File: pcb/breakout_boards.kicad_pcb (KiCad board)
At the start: 2 copper layers, 26.8 x 20 mm, 91 parts, among them J1 Conn_01x04, J2 Conn_01x04, J3 Conn_01x04, J4 Conn_01x04, J5 Conn_01x04, J6 Conn_01x04, J7 Conn_01x04, J8 Conn_01x04, J9 Conn_01x04, SW1 SW_Push_45deg, SW10 SW_Push_45deg, SW11 SW_Push_45deg, SW12 SW_Push_45deg, SW13 SW_Push_45deg, SW14 SW_Push_45deg, SW15 SW_Push_45deg, SW16 SW_Push_45deg, SW17 SW_Push_45deg, SW18 SW_Push_45deg, SW19 SW_Push_45deg, SW2 SW_Push_45deg, SW20 SW_Push_45deg, SW21 SW_Push_45deg, SW22 SW_Push_45deg, SW23 SW_Push_45deg, SW24 SW_Push_45deg, SW25 SW_Push_45deg, SW26 SW_Push_45deg, SW27 SW_Push_45deg, SW28 SW_Push_45deg, SW29 SW_Push_45deg, SW3 SW_Push_45deg, SW30 SW_Push_45deg, SW31 SW_Push_45deg, SW32 SW_Push_45deg, SW4 SW_Push_45deg, SW5 SW_Push_45deg, SW6 SW_Push_45deg, SW7 SW_Push_45deg, SW8 SW_Push_45deg, SW9 SW_Push_45deg

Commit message: almost done
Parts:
- removed J2: Conn_01x04, Connector_PinHeader_2.54mm:PinHeader_1x04_P2.54mm_Vertical
- added H2: MountingHole, Panelization:mouse-bite-3mm-slot, F.Cu at (45.5, 22.0)
- added H3: MountingHole, Panelization:mouse-bite-3mm-slot, F.Cu at (21.8, 33.2)
- added H4: MountingHole, Panelization:mouse-bite-3mm-slot, F.Cu at (22.0, 41.0)
- added H5: MountingHole, Panelization:mouse-bite-3mm-slot, F.Cu at (50.8, 41.0)
- added H6: MountingHole, Panelization:mouse-bite-3mm-slot, F.Cu at (38.0, 31.2)
- added H7: MountingHole, Panelization:mouse-bite-3mm-slot, F.Cu at (38.0, 41.0)
- added H8: MountingHole, Panelization:mouse-bite-3mm-slot, F.Cu at (45.5, 35.8)
- J1: value Conn_01x04 -> Conn_01x05; footprint Connector_PinHeader_2.54mm:PinHeader_1x04_P2.54mm_Vertical -> Connector_PinHeader_2.54mm:PinHeader_1x05_P2.54mm_Vertical
- J6, J7: moved to B.Cu
- moved SW8 132.3 mm to (47.0, 57.4)
- moved SW7 126.6 mm to (37.0, 57.4)
- moved J6 124.6 mm to (31.4, 44.5), turned to -90 degrees
- moved SW6 122.0 mm to (27.0, 57.4)
- moved SW16 119.7 mm to (47.0, 73.3)
- moved SW5 118.8 mm to (17.0, 57.4)
- moved SW15 115.5 mm to (37.0, 73.3)
- moved SW14 112.6 mm to (27.0, 73.3)
- moved SW13 111.3 mm to (17.0, 73.3)
- moved SW4 106.8 mm to (47.0, 49.4)
- moved SW3 101.9 mm to (37.0, 49.4)
- moved J7 100.8 mm to (31.4, 82.6), turned to -90 degrees
- moved SW2 98.5 mm to (27.0, 49.4)
- moved SW1 96.8 mm to (17.0, 49.4)
- moved SW12 95.2 mm to (47.0, 65.3)
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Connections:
- D2 pad 1: Net-(D2-K) -> Net-(D1-K)
- D3 pad 1: Net-(D3-K) -> Net-(D1-K)
- D4 pad 1: Net-(D4-K) -> Net-(D1-K)
- J1 pad 1: Net-(J1-Pin_1) -> Net-(D1-K)
- J4 pad 1: Net-(J4-Pin_1) -> /led_matrix.r3
- J4 pad 2: Net-(J4-Pin_2) -> /led_matrix.r2
- J4 pad 3: Net-(J4-Pin_3) -> /led_matrix.r1
- J4 pad 4: Net-(J4-Pin_4) -> /led_matrix.r0
- J5 pad 1: /led_matrix.c3 -> Net-(J5-Pin_1)
- J5 pad 2: /led_matrix.c2 -> Net-(J5-Pin_2)
- J5 pad 3: /led_matrix.c1 -> Net-(J5-Pin_3)
- J5 pad 4: /led_matrix.c0 -> Net-(J5-Pin_4)
- R1 pad 1: Net-(J1-Pin_4) -> Net-(J1-Pin_2)
- R3 pad 1: Net-(J1-Pin_2) -> Net-(J1-Pin_4)
- R4 pad 1: Net-(J1-Pin_1) -> Net-(J1-Pin_5)
- R5 pad 1: Net-(J4-Pin_3) -> /led_matrix.c1
- R5 pad 2: /led_matrix.r1 -> Net-(J5-Pin_3)
- R7 pad 1: Net-(J4-Pin_2) -> /led_matrix.c2
- R7 pad 2: /led_matrix.r2 -> Net-(J5-Pin_2)
- R8 pad 1: Net-(J4-Pin_1) -> /led_matrix.c3
- R8 pad 2: /led_matrix.r3 -> Net-(J5-Pin_1)
- R9 pad 1: Net-(J4-Pin_4) -> /led_matrix.c0
- R9 pad 2: /led_matrix.r0 -> Net-(J5-Pin_4)
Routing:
- net /keyboard_matrix.r3: track 0.00 -> 68.8 mm, vias 0 -> 1
- net /keyboard_matrix.c0: track 0.00 -> 67.0 mm
- net /keyboard_matrix.c3: track 0.00 -> 66.7 mm
- net /keyboard_matrix.c2: track 0.00 -> 61.6 mm
- net /keyboard_matrix.c1: track 0.00 -> 61.2 mm
- net /keyboard_matrix.r2: track 0.00 -> 57.9 mm, vias 0 -> 1
- net /keyboard_matrix.r1: track 0.00 -> 55.4 mm, vias 0 -> 1
- net /keyboard_matrix.r0: track 0.00 -> 50.3 mm, vias 0 -> 1
- net /led_matrix.c0: track 39.1 -> 13.4 mm, vias 1 -> 0
- net Net-(J5-Pin_4): track 0.00 -> 21.4 mm, vias 0 -> 1
- net /led_matrix.c1: track 34.7 -> 13.4 mm, vias 1 -> 0
- net Net-(D1-K): track 3.01 -> 22.3 mm
- net Net-(J5-Pin_3): track 0.00 -> 16.2 mm, vias 0 -> 1
- net /led_matrix.c3: track 0.00 -> 12.8 mm
- net Net-(J5-Pin_2): track 0.00 -> 10.7 mm, vias 0 -> 1
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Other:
- board size 26.8 x 20 mm -> 52.2 x 69.8 mm
- board text added: "4x4"
- board text added: "KEYBOARD"
- board text added: "LED MATRIX"
- board text added: "RGB LED"

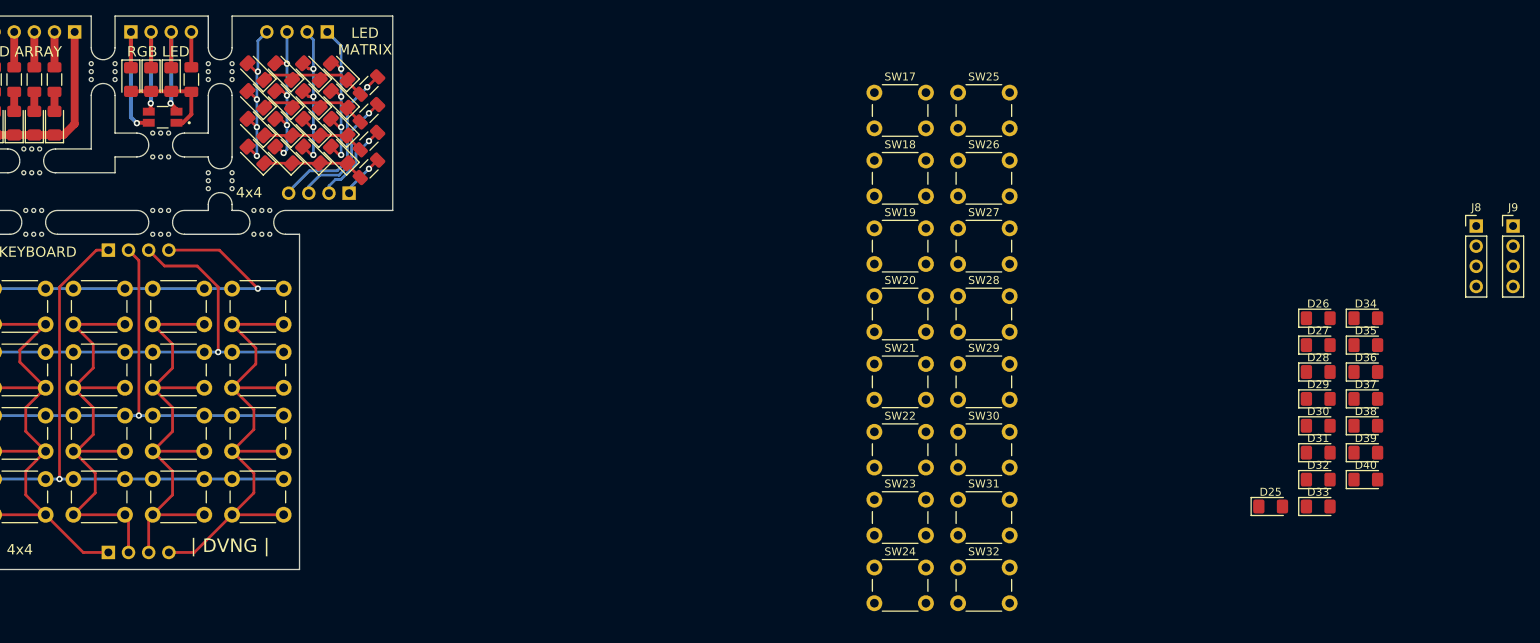
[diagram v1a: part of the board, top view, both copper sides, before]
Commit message: added all basic breakout boards as before
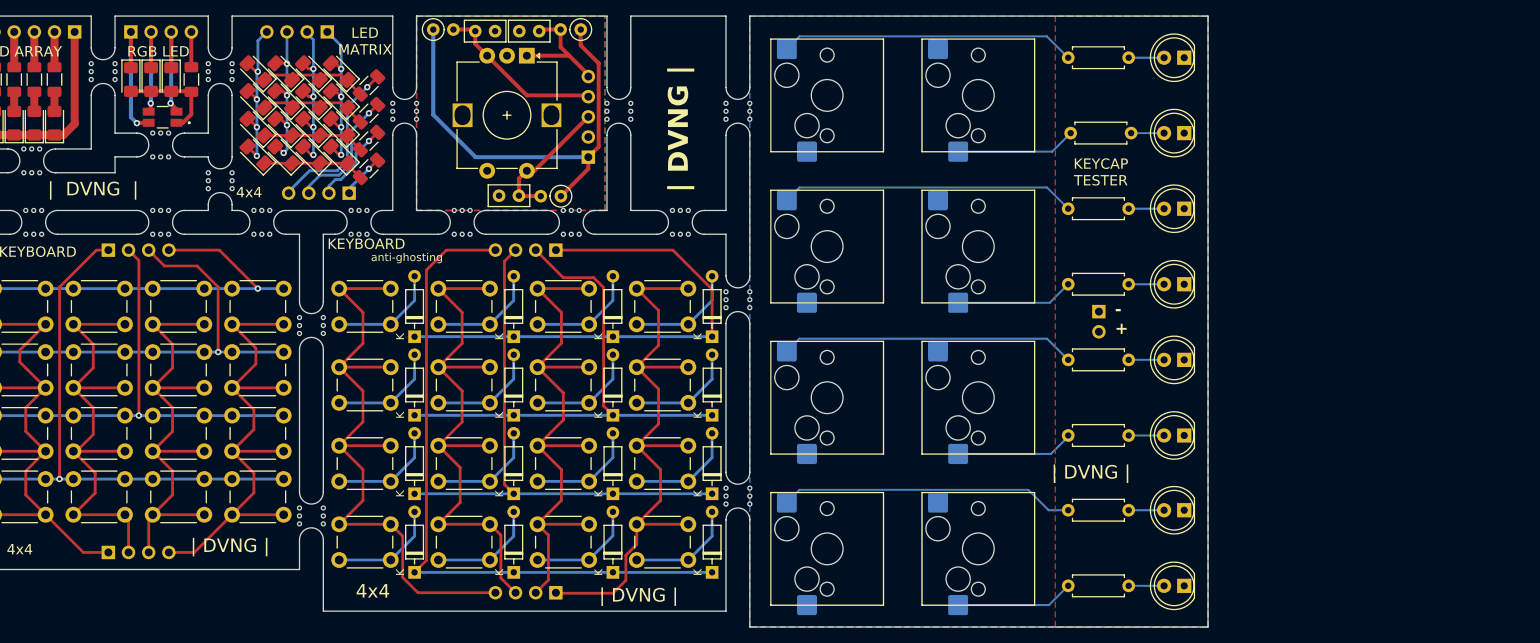
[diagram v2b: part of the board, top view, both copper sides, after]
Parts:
- added C1: 10n, Capacitor_THT:C_Disc_D5.0mm_W2.5mm_P2.50mm, F.Cu at (83.2, 16.9)
- added C2: 10n, Capacitor_THT:C_Disc_D5.0mm_W2.5mm_P2.50mm, F.Cu at (80.2, 16.9)
- added C3: 10n, Capacitor_THT:C_Disc_D5.0mm_W2.5mm_P2.50mm, F.Cu at (83.2, 37.6)
- added D41: LED_Small, LED_THT:LED_D5.0mm_Clear, F.Cu at (167.0, 86.8)
- added D42: LED_Small, LED_THT:LED_D5.0mm_Clear, F.Cu at (167.0, 77.3)
- added D43: LED_Small, LED_THT:LED_D5.0mm_Clear, F.Cu at (167.0, 67.9)
- added D44: LED_Small, LED_THT:LED_D5.0mm_Clear, F.Cu at (167.0, 58.3)
- added D45: LED_Small, LED_THT:LED_D5.0mm_Clear, F.Cu at (167.0, 48.8)
- added D46: LED_Small, LED_THT:LED_D5.0mm_Clear, F.Cu at (167.0, 39.3)
- added D47: LED_Small, LED_THT:LED_D5.0mm_Clear, F.Cu at (167.0, 29.8)
- added D48: LED_Small, LED_THT:LED_D5.0mm_Clear, F.Cu at (167.0, 20.2)
- added H10: MountingHole, Panelization:mouse-bite-3mm-slot, F.Cu at (57.0, 78.0)
- added H11: MountingHole, Panelization:mouse-bite-3mm-slot, F.Cu at (63.0, 41.0)
- added H12: MountingHole, Panelization:mouse-bite-3mm-slot, F.Cu at (68.8, 27.0)
- added H13: MountingHole, Panelization:mouse-bite-3mm-slot, F.Cu at (103.5, 41.0)
- added H14: MountingHole, Panelization:mouse-bite-3mm-slot, F.Cu at (76.0, 41.0)
- added H15: MountingHole, Panelization:mouse-bite-3mm-slot, F.Cu at (89.8, 41.0)
- added H17: MountingHole, Panelization:mouse-bite-3mm-slot, F.Cu at (110.8, 27.0)
- added H19: MountingHole, Panelization:mouse-bite-3mm-slot, F.Cu at (95.8, 27.0)
- added H20: MountingHole, Panelization:mouse-bite-3mm-slot, F.Cu at (110.8, 50.8)
- added H21: MountingHole, Panelization:mouse-bite-3mm-slot, F.Cu at (110.8, 75.5)
- added H9: MountingHole, Panelization:mouse-bite-3mm-slot, F.Cu at (57.0, 54.0)
- added J10: Conn_01x05, Connector_PinHeader_2.54mm:PinHeader_1x05_P2.54mm_Vertical, B.Cu at (91.9, 32.8)
- added J2: Conn_01x02, Connector_PinHeader_2.54mm:PinHeader_1x02_P2.54mm_Vertical, B.Cu at (156.2, 52.2)
- added R10: R_Small, Resistor_THT:R_Axial_DIN0207_L6.3mm_D2.5mm_P7.62mm_Horizontal, F.Cu at (160.0, 86.8)
- added R11: R_Small, Resistor_THT:R_Axial_DIN0207_L6.3mm_D2.5mm_P7.62mm_Horizontal, F.Cu at (160.0, 77.3)
- added R12: R_Small, Resistor_THT:R_Axial_DIN0207_L6.3mm_D2.5mm_P7.62mm_Horizontal, F.Cu at (160.0, 67.9)
- added R13: R_Small, Resistor_THT:R_Axial_DIN0207_L6.3mm_D2.5mm_P7.62mm_Horizontal, F.Cu at (160.0, 58.3)
- added R14: R_Small, Resistor_THT:R_Axial_DIN0207_L6.3mm_D2.5mm_P7.62mm_Horizontal, F.Cu at (160.0, 48.8)
- added R15: R_Small, Resistor_THT:R_Axial_DIN0207_L6.3mm_D2.5mm_P7.62mm_Horizontal, F.Cu at (160.0, 39.3)
- added R16: R_Small, Resistor_THT:R_Axial_DIN0207_L6.3mm_D2.5mm_P7.62mm_Horizontal, F.Cu at (160.3, 29.8)
- added R17: R_Small, Resistor_THT:R_Axial_DIN0207_L6.3mm_D2.5mm_P7.62mm_Horizontal, F.Cu at (160.0, 20.2)
- added R18: 10K, Resistor_THT:R_Axial_DIN0207_L6.3mm_D2.5mm_P2.54mm_Vertical, F.Cu at (90.9, 16.7)
- added R19: 10K, Resistor_THT:R_Axial_DIN0207_L6.3mm_D2.5mm_P2.54mm_Vertical, F.Cu at (88.4, 37.7)
- added R20: 10K, Resistor_THT:R_Axial_DIN0207_L6.3mm_D2.5mm_P2.54mm_Vertical, F.Cu at (72.4, 16.7)
- added SW33: SW_Push, Button_Switch_Keyboard:SW_Hotswap_Kailh_MX_1.00u, F.Cu at (122.0, 82.2)
- added SW34: SW_Push, Button_Switch_Keyboard:SW_Hotswap_Kailh_MX_1.00u, F.Cu at (141.1, 82.2)
- added SW35: SW_Push, Button_Switch_Keyboard:SW_Hotswap_Kailh_MX_1.00u, F.Cu at (122.0, 63.1)
- added SW36: SW_Push, Button_Switch_Keyboard:SW_Hotswap_Kailh_MX_1.00u, F.Cu at (141.1, 63.1)
- added SW37: SW_Push, Button_Switch_Keyboard:SW_Hotswap_Kailh_MX_1.00u, F.Cu at (122.0, 44.0)
- added SW38: SW_Push, Button_Switch_Keyboard:SW_Hotswap_Kailh_MX_1.00u, F.Cu at (141.1, 44.0)
- added SW39: SW_Push, Button_Switch_Keyboard:SW_Hotswap_Kailh_MX_1.00u, F.Cu at (122.0, 25.0)
- added SW40: SW_Push, Button_Switch_Keyboard:SW_Hotswap_Kailh_MX_1.00u, F.Cu at (141.1, 25.0)
- added SW41: RotaryEncoder_Switch_MP, Rotary_Encoder:RotaryEncoder_Alps_EC12E-Switch_Vertical_H20mm, F.Cu at (84.2, 20.0)
- D1, D2, D3, D4, D5, D7, D8: footprint Diode_SMD:D_1206_3216Metric_Pad1.42x1.75mm_HandSolder -> LED_SMD:LED_1206_3216Metric_Pad1.42x1.75mm_HandSolder
- D25, D26, D27, D28, D29, D30, D31, D32, D33, D34, D35, D36, D37, D38, D39, D40: footprint Diode_SMD:D_1206_3216Metric_Pad1.42x1.75mm_HandSolder -> Diode_THT:D_DO-35_SOD27_P7.62mm_Horizontal
- J8, J9: moved to B.Cu
- moved J9 129.2 mm to (87.8, 87.7), turned to 90 degrees
- moved D28 116.7 mm to (70.0, 85.1), turned to 90 degrees
- moved J8 116.0 mm to (87.8, 44.5), turned to 90 degrees
- moved D27 115.4 mm to (70.0, 75.2), turned to 90 degrees
- moved D26 114.5 mm to (70.0, 65.3), turned to 90 degrees
- moved D25 110.0 mm to (70.0, 55.4), turned to 90 degrees
- moved D32 102.1 mm to (82.5, 85.1), turned to 90 degrees
- moved D29 101.7 mm to (82.5, 55.4), turned to 90 degrees
- moved D31 101.5 mm to (82.5, 75.2), turned to 90 degrees
- moved D30 101.4 mm to (82.5, 65.3), turned to 90 degrees
- moved D36 98.2 mm to (95.0, 85.1), turned to 90 degrees
- moved D35 96.7 mm to (95.0, 75.2), turned to 90 degrees
- moved D34 95.7 mm to (95.0, 65.3), turned to 90 degrees
- moved D33 91.4 mm to (95.0, 55.4), turned to 90 degrees
- moved D40 83.2 mm to (107.5, 85.1), turned to 90 degrees
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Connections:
- SW29 pad 1: /keyboard_noghost_matrix.r2 -> /keyboard_noghost_matrix.r3
- SW30 pad 1: /keyboard_noghost_matrix.r2 -> /keyboard_noghost_matrix.r3
- SW31 pad 1: /keyboard_noghost_matrix.r2 -> /keyboard_noghost_matrix.r3
- SW32 pad 1: /keyboard_noghost_matrix.r2 -> /keyboard_noghost_matrix.r3
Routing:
- net /keyboard_noghost_matrix.c0: track 0.00 -> 86.0 mm
- net /keyboard_noghost_matrix.r0: track 0.00 -> 83.0 mm
- net /keyboard_noghost_matrix.r3: track 0.00 -> 79.9 mm
- net /keyboard_noghost_matrix.r2: track 0.00 -> 73.2 mm
- net /keyboard_noghost_matrix.r1: track 0.00 -> 72.9 mm
- net /keyboard_noghost_matrix.c1: track 0.00 -> 69.3 mm
- net /keyboard_noghost_matrix.c3: track 0.00 -> 65.2 mm
- net /keyboard_noghost_matrix.c2: track 0.00 -> 64.6 mm
- net /single_encoder.vcc: track 0.00 -> 56.4 mm
- net Net-(R17-Pad2): track 0.00 -> 37.2 mm
- net Net-(R15-Pad2): track 0.00 -> 37.2 mm
- net Net-(R13-Pad2): track 0.00 -> 37.2 mm
- net Net-(R11-Pad2): track 0.00 -> 37.2 mm
- net /single_encoder.b: track 0.00 -> 21.4 mm
- net /single_encoder.sw: track 0.00 -> 16.9 mm
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- added copper zone on B.Cu, net /keycap_tester.vcc
- added copper zone on F.Cu, net /keycap_tester.vss
- added copper zone on B.Cu, net /single_encoder.vss
- added copper zone on F.Cu, net /single_encoder.vss
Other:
- board size 52.2 x 69.8 mm -> 155 x 77 mm
- board text added: "- +"
- board text added: "KEYCAP TESTER"
- board text added: "anti-ghosting"
